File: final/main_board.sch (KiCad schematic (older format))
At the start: 81 parts, among them J1 USB_microB_2040002-1, J2 Arduino_ICSP, J3 E-INK DISPLAY, J4 BT CONFIG, J5 Conn_01x02_Male, J6 Conn_01x15_Male, J7 Conn_01x15_Male, SW1 SW_DIP_x01, U1 MCP1702T-3302E/CBCT-ND, U10 BQ27441-G1, U11 NC7SZ04P5X, U2 TXS0108EPW, U3 FT232RL, U4 TPS61200DRC, U5 TXS0104E, U6 TPS2113ADRBR, U7 RN4871, U8 ATMEGA328PB-ANR, U9 BQ24075, Y1 16MHz

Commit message: Footprint Assigned
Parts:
- J5: footprint (none) -> Connector_PinHeader_2.54mm:PinHeader_1x02_P2.54mm_Vertical
- R1, R12, R13, R2: footprint (none) -> Resistor_SMD:R_0603_1608Metric
- U3: footprint (none) -> mp3b:FT232RQ
- U8: footprint (none) -> mp3b:Atmega328pb
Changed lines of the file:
@@
 EESchema Schematic File Version 4
 LIBS:main_board-cache
-EELAYER 26 0
+EELAYER 29 0
 EELAYER END
 $Descr C 22000 17000
@@
 F 0 "U8" H 10250 9365 50  0000 C CNN
 F 1 "ATMEGA328PB-ANR" H 10250 9274 50  0000 C CNN
-F 2 "" H 10250 7000 50  0001 C CNN
+F 2 "mp3b:Atmega328pb" H 10250 7000 50  0001 C CNN
 F 3 "" H 10250 7000 50  0001 C CNN
 	1    10250 7200
@@
 F 0 "U3" H 4950 8165 50  0000 C CNN
 F 1 "FT232RL" H 4950 8074 50  0000 C CNN
-F 2 "" H 4950 7550 50  0001 C CNN
+F 2 "mp3b:FT232RQ" H 4950 7550 50  0001 C CNN
 F 3 "" H 4950 7550 50  0001 C CNN
 	1    4950 6600
@@
 F 0 "R1" H 3840 10346 50  0000 L CNN
 F 1 "47K" H 3840 10255 50  0000 L CNN
-F 2 "" V 3700 10300 50  0001 C CNN
+F 2 "Resistor_SMD:R_0603_1608Metric" V 3700 10300 50  0001 C CNN
 F 3 "~" H 3770 10300 50  0001 C CNN
 	1    3770 10300
@@
 F 0 "R12" H 12200 11456 50  0000 L CNN
 F 1 "1K" H 12200 11365 50  0000 L CNN
-F 2 "" V 12060 11410 50  0001 C CNN
+F 2 "Resistor_SMD:R_0603_1608Metric" V 12060 11410 50  0001 C CNN
 F 3 "~" H 12130 11410 50  0001 C CNN
 	1    12130 11410
@@
 F 0 "R13" H 12910 11166 50  0000 L CNN
 F 1 "1K" H 12910 11075 50  0000 L CNN
-F 2 "" V 12770 11120 50  0001 C CNN
+F 2 "Resistor_SMD:R_0603_1608Metric" V 12770 11120 50  0001 C CNN
 F 3 "~" H 12840 11120 50  0001 C CNN
 	1    12840 11120
@@
 F 0 "R2" H 8330 11486 50  0000 L CNN
 F 1 "47K" H 8330 11395 50  0000 L CNN
-F 2 "" V 8190 11440 50  0001 C CNN
+F 2 "Resistor_SMD:R_0603_1608Metric" V 8190 11440 50  0001 C CNN
 F 3 "~" H 8260 11440 50  0001 C CNN
 	1    8260 11440
@@
 F 0 "J5" H 19773 6680 50  0000 R CNN
 F 1 "Conn_01x02_Male" H 19773 6771 50  0000 R CNN
-F 2 "" H 19800 6800 50  0001 C CNN
+F 2 "Connector_PinHeader_2.54mm:PinHeader_1x02_P2.54mm_Vertical" H 19800 6800 50  0001 C CNN
 F 3 "~" H 19800 6800 50  0001 C CNN
 	1    19800 6800

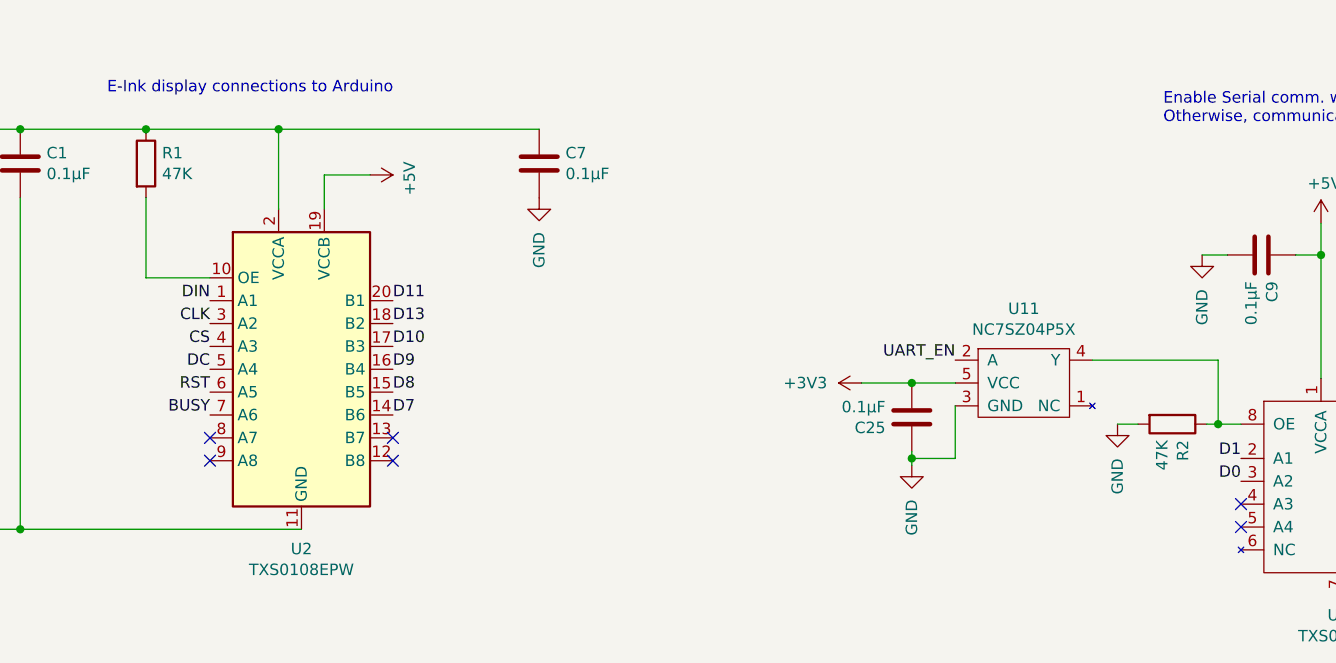
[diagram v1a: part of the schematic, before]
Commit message: Change pull up/down resistor values for logic level enable pins
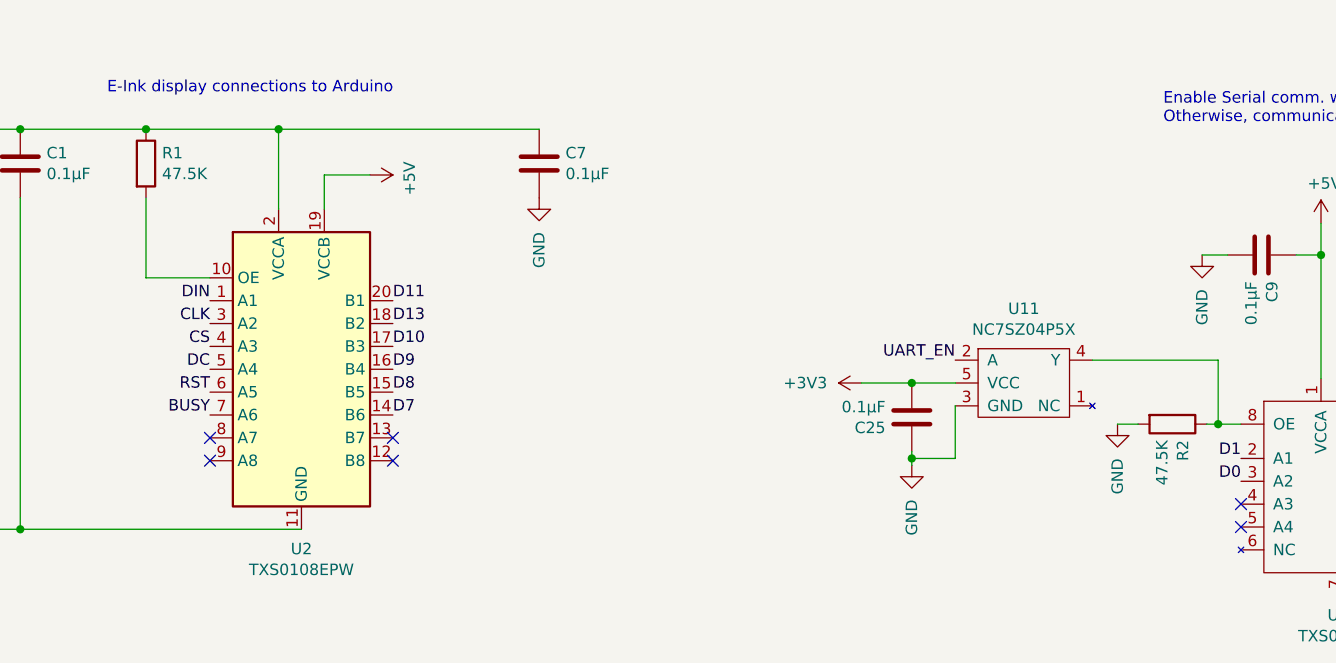
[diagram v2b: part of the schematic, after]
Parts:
- R1, R2: value 47K -> 47.5K
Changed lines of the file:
@@
 EESchema Schematic File Version 4
 LIBS:main_board-cache
-EELAYER 29 0
+EELAYER 26 0
 EELAYER END
 $Descr C 22000 17000
@@
 P 3770 10300
 F 0 "R1" H 3840 10346 50  0000 L CNN
-F 1 "47K" H 3840 10255 50  0000 L CNN
+F 1 "47.5K" H 3840 10255 50  0000 L CNN
 F 2 "Resistor_SMD:R_0603_1608Metric" V 3700 10300 50  0001 C CNN
 F 3 "~" H 3770 10300 50  0001 C CNN
@@
 P 8260 11440
 F 0 "R2" H 8330 11486 50  0000 L CNN
-F 1 "47K" H 8330 11395 50  0000 L CNN
+F 1 "47.5K" H 8330 11395 50  0000 L CNN
 F 2 "Resistor_SMD:R_0603_1608Metric" V 8190 11440 50  0001 C CNN
 F 3 "~" H 8260 11440 50  0001 C CNN

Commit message: Assign new footprint to capacitor
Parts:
- C23: footprint Capacitor_SMD:C_0603_1608Metric -> Capacitor_SMD:C_0402_1005Metric
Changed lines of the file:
@@
 F 0 "C23" H 17415 3396 50  0000 L CNN
 F 1 "0.47µF" H 17415 3305 50  0000 L CNN
-F 2 "Capacitor_SMD:C_0603_1608Metric" H 17338 3200 50  0001 C CNN
+F 2 "Capacitor_SMD:C_0402_1005Metric" H 17338 3200 50  0001 C CNN
 F 3 "~" H 17300 3350 50  0001 C CNN
 	1    17300 3350

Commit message: footprint
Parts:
- J4: footprint (none) -> Connector_PinHeader_2.54mm:PinHeader_1x08_P2.54mm_Vertical
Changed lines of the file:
@@
 EESchema Schematic File Version 4
 LIBS:main_board-cache
-EELAYER 26 0
+EELAYER 29 0
 EELAYER END
 $Descr C 22000 17000
@@
 F 0 "J4" H 19763 12783 50  0000 R CNN
 F 1 "BT CONFIG" H 19763 12692 50  0000 R CNN
-F 2 "" H 19790 12810 50  0001 C CNN
+F 2 "Connector_PinHeader_2.54mm:PinHeader_1x08_P2.54mm_Vertical" H 19790 12810 50  0001 C CNN
 F 3 "~" H 19790 12810 50  0001 C CNN
 	1    19790 12810

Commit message: added new footprints and assignments
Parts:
- U11: footprint (none) -> mp3b:NC7SZ04P5X
- U4: footprint Package_SON:Texas_S-PVSON-N10_ThermalVias -> mp3b:TPS61200DRC
- U6: footprint (none) -> mp3b:TPS2113ADRBR
- U9: footprint (none) -> mp3b:BQ24075
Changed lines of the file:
@@
 F 0 "U6" H 7950 3887 60  0000 C CNN
 F 1 "TPS2113ADRBR" H 7950 3781 60  0000 C CNN
-F 2 "" H 7950 3450 60  0001 C CNN
+F 2 "mp3b:TPS2113ADRBR" H 7950 3450 60  0001 C CNN
 F 3 "" H 7950 3450 60  0001 C CNN
 	1    7950 3300
@@
 F 0 "U9" H 12200 4028 50  0000 C CNN
 F 1 "BQ24075" H 12200 3937 50  0000 C CNN
-F 2 "" H 12450 2700 50  0001 L CNN
+F 2 "mp3b:BQ24075" H 12450 2700 50  0001 L CNN
 F 3 "http://www.ti.com/lit/ds/symlink/bq24075.pdf" H 12400 3450 50  0001 C CNN
 	1    12200 3250
@@
 F 0 "U11" H 7610 11585 50  0000 C CNN
 F 1 "NC7SZ04P5X" H 7610 11494 50  0000 C CNN
-F 2 "" H 7610 11260 50  0001 C CNN
+F 2 "mp3b:NC7SZ04P5X" H 7610 11260 50  0001 C CNN
 F 3 "" H 7610 11260 50  0001 C CNN
 	1    7610 11260
@@
 F 0 "U4" H 4750 3667 50  0000 C CNN
 F 1 "TPS61200DRC" H 4750 3576 50  0000 C CNN
-F 2 "Package_SON:Texas_S-PVSON-N10_ThermalVias" H 4750 2750 50  0001 C CNN
+F 2 "mp3b:TPS61200DRC" H 4750 2750 50  0001 C CNN
 F 3 "http://www.ti.com/lit/ds/symlink/tps61200.pdf" H 4750 3200 50  0001 C CNN
 	1    4750 3200

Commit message: Assigned footprints
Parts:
- L1: footprint (none) -> mp3b:CDRH2D18HP
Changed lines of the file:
@@
 EESchema Schematic File Version 4
 LIBS:main_board-cache
-EELAYER 29 0
+EELAYER 26 0
 EELAYER END
 $Descr C 22000 17000
@@
 F 0 "L1" H 4650 2815 50  0000 C CNN
 F 1 "4.7uH" H 4650 2724 50  0000 C CNN
-F 2 "" H 4650 2600 50  0001 C CNN
+F 2 "mp3b:CDRH2D18HP" H 4650 2600 50  0001 C CNN
 F 3 "http://products.sumida.com/products/pdf/CDRH2D18HP.pdf" H 4650 2600 50  0001 C CNN
 	1    4650 2600

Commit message: Footprint additions
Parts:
- J5: footprint Connector_PinHeader_2.54mm:PinHeader_1x02_P2.54mm_Vertical -> mp3b:JST-2-SMD
- SW1: footprint (none) -> mp3b:KAE01SGGt
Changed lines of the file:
@@
 F 0 "J5" H 19773 6680 50  0000 R CNN
 F 1 "Conn_01x02_Male" H 19773 6771 50  0000 R CNN
-F 2 "Connector_PinHeader_2.54mm:PinHeader_1x02_P2.54mm_Vertical" H 19800 6800 50  0001 C CNN
+F 2 "mp3b:JST-2-SMD" H 19800 6800 50  0001 C CNN
 F 3 "~" H 19800 6800 50  0001 C CNN
 	1    19800 6800
@@
 F 0 "SW1" H 1850 2317 50  0000 C CNN
 F 1 "SW_DIP_x01" H 1850 2226 50  0000 C CNN
-F 2 "" H 1850 2050 50  0001 C CNN
+F 2 "mp3b:KAE01SGGt" H 1850 2050 50  0001 C CNN
 F 3 "" H 1850 2050 50  0001 C CNN
 	1    1850 2050
